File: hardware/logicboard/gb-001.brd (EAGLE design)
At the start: 100 x 75 mm, 2 parts

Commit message: Expanded logicboard.
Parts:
- removed SV1: (no value), con-ml:ML16L
- added SV0: (no value), con-ml:ML34L
- added SV2: (no value), con-ml:ML20L
- added SV3: (no value), con-ml:ML14L
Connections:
- removed net ANLG0R: SV1.3
- removed net ANLG1R: SV1.7
- removed net ANLG2R: SV1.11
- removed net ANLG3R: SV1.15
- removed net DTCT0: SV1.2
- removed net DTCT1: SV1.6
- removed net DTCT2: SV1.10
- removed net DTCT3: SV1.14
- removed net GND: SV1.1, SV1.13, SV1.5, SV1.9
- removed net VCC/2: SV1.12, SV1.16, SV1.4, SV1.8
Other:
- board size 100 x 75 mm -> 100 x 76 mm
- board text added: "Designed for Takachi PF13-3-9"
- board text removed: "Designed for Takachi PF13-4-9"
- board text removed: "GeekPort II"
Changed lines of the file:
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@@
 <setting verticaltext="up"/>
 </settings>
-<grid distance="0.5" unitdist="mm" unit="mm" style="lines" multiple="2" display="yes" altdistance="50" altunitdist="mil" altunit="mil"/>
+<grid distance="1" unitdist="mm" unit="mm" style="lines" multiple="2" display="yes" altdistance="50" altunitdist="mil" altunit="mil"/>
 <layers>
 <layer number="1" name="Top" color="4" fill="1" visible="yes" active="yes"/>
@@
 <layer number="39" name="tKeepout" color="4" fill="11" visible="yes" active="yes"/>
 <layer number="40" name="bKeepout" color="1" fill="11" visible="yes" active="yes"/>
-<layer number="41" name="tRestrict" color="4" fill="10" visible="yes" active="yes"/>
-<layer number="42" name="bRestrict" color="1" fill="10" visible="yes" active="yes"/>
+<layer number="41" name="tRestrict" color="4" fill="10" visible="no" active="yes"/>
+<layer number="42" name="bRestrict" color="1" fill="10" visible="no" active="yes"/>
 <layer number="43" name="vRestrict" color="2" fill="10" visible="yes" active="yes"/>
 <layer number="44" name="Drills" color="7" fill="1" visible="no" active="yes"/>
@@
 <board>
 <plain>
-<wire x1="95" y1="75" x2="5" y2="75" width="0" layer="20"/>
-<wire x1="5" y1="75" x2="4" y2="74" width="0" layer="20" curve="90"/>
-<wire x1="4" y1="74" x2="4" y2="65" width="0" layer="20"/>
+<wire x1="95" y1="75.5" x2="5" y2="75.5" width="0" layer="20"/>
+<wire x1="5" y1="75.5" x2="4" y2="74.5" width="0" layer="20" curve="90"/>
+<wire x1="4" y1="74.5" x2="4" y2="65" width="0" layer="20"/>
 <wire x1="2.5" y1="63.5" x2="1" y2="63.5" width="0" layer="20"/>
 <wire x1="1" y1="63.5" x2="0" y2="62.5" width="0" layer="20" curve="90"/>
@@
 <wire x1="0" y1="12.5" x2="1" y2="11.5" width="0" layer="20" curve="90"/>
 <wire x1="1" y1="11.5" x2="2.5" y2="11.5" width="0" layer="20"/>
-<wire x1="4" y1="10" x2="4" y2="1" width="0" layer="20"/>
-<wire x1="4" y1="1" x2="5" y2="0" width="0" layer="20" curve="90"/>
-<wire x1="5" y1="0" x2="95" y2="0" width="0" layer="20"/>
-<wire x1="95" y1="0" x2="96" y2="1.5" width="0" layer="20" curve="90"/>
-<wire x1="96" y1="1.5" x2="96" y2="10" width="0" layer="20"/>
+<wire x1="4" y1="10" x2="4" y2="0.5" width="0" layer="20"/>
+<wire x1="4" y1="0.5" x2="5" y2="-0.5" width="0" layer="20" curve="90"/>
+<wire x1="5" y1="-0.5" x2="95" y2="-0.5" width="0" layer="20"/>
+<wire x1="95" y1="-0.5" x2="96" y2="0.5" width="0" layer="20" curve="90"/>
+<wire x1="96" y1="0.5" x2="96" y2="10" width="0" layer="20"/>
 <wire x1="97.5" y1="11.5" x2="99" y2="11.5" width="0" layer="20"/>
 <wire x1="99" y1="11.5" x2="100" y2="12.5" width="0" layer="20" curve="90"/>
@@
 <wire x1="100" y1="62.5" x2="99" y2="63.5" width="0" layer="20" curve="90"/>
 <wire x1="99" y1="63.5" x2="97.5" y2="63.5" width="0" layer="20"/>
-<wire x1="96" y1="65" x2="96" y2="74" width="0" layer="20"/>
-<wire x1="96" y1="74" x2="95" y2="75" width="0" layer="20" curve="90"/>
+<wire x1="96" y1="65" x2="96" y2="74.5" width="0" layer="20"/>
+<wire x1="96" y1="74.5" x2="95" y2="75.5" width="0" layer="20" curve="90"/>
 <hole x="93.5" y="61" drill="2.5"/>
 <circle x="6.5" y="14" radius="2" width="0.2" layer="42"/>
@@
 <text x="4.5" y="6" size="1" layer="25" align="center-left">Designed for
 Takachi
-PF13-4-9</text>
-<text x="90" y="70.5" size="1" layer="25" rot="R90" align="center">GeekPort II</text>
-<hole x="87.5" y="70.5" drill="2.7"/>
-<hole x="62.5" y="70.5" drill="2.7"/>
-<circle x="87.5" y="70.5" radius="2" width="0.2" layer="41"/>
-<circle x="62.5" y="70.5" radius="2" width="0.2" layer="41"/>
-<circle x="87.5" y="70.5" radius="2" width="0.2" layer="42"/>
-<circle x="62.5" y="70.5" radius="2" width="0.2" layer="42"/>
+PF13-3-9</text>
 <text x="93.5" y="11.5" size="1" layer="25" align="center">4-M2.3</text>
 </plain>
@@
 <elements>
 <element name="U$1" library="pineapple" package="PINEAPPLE450_SILK" value="PINEAPPLE450_SILK" x="8.5" y="34" smashed="yes"/>
-<element name="SV1" library="con-ml" library_urn="urn:adsk.eagle:library:164" package="ML16L" package3d_urn="urn:adsk.eagle:package:8682/1" value="" x="75" y="64" smashed="yes">
-<attribute name="MF" value="" x="75" y="64" size="1.778" layer="27" display="off"/>
-<attribute name="MPN" value="" x="75" y="64" size="1.778" layer="27" display="off"/>
-<attribute name="NAME" x="87.5" y="64" size="1" layer="25" ratio="10" align="center"/>
-<attribute name="OC_FARNELL" value="unknown" x="75" y="64" size="1.778" layer="27" display="off"/>
-<attribute name="OC_NEWARK" value="unknown" x="75" y="64" size="1.778" layer="27" display="off"/>
-<attribute name="POPULARITY" value="0" x="75" y="64" size="1.778" layer="27" display="off"/>
-<attribute name="VALUE" x="74.9746" y="75.43" size="1.778" layer="27" ratio="10"/>
+<element name="SV0" library="con-ml" library_urn="urn:adsk.eagle:library:164" package="ML34L" package3d_urn="urn:adsk.eagle:package:8689/1" value="" x="50" y="11" smashed="yes" rot="R180">
+<attribute name="MF" value="" x="50" y="11" size="1.778" layer="27" rot="R180" display="off"/>
+<attribute name="MPN" value="" x="50" y="11" size="1.778" layer="27" rot="R180" display="off"/>
+<attribute name="NAME" x="75.4254" y="-0.43" size="1.778" layer="25" ratio="10" rot="R180"/>
+<attribute name="OC_FARNELL" value="unknown" x="50" y="11" size="1.778" layer="27" rot="R180" display="off"/>
+<attribute name="OC_NEWARK" value="unknown" x="50" y="11" size="1.778" layer="27" rot="R180" display="off"/>
+<attribute name="POPULARITY" value="0" x="50" y="11" size="1.778" layer="27" rot="R180" display="off"/>
+<attribute name="VALUE" x="60.1854" y="-0.43" size="1.778" layer="27" ratio="10" rot="R180"/>
+</element>
+<element name="SV2" library="con-ml" library_urn="urn:adsk.eagle:library:164" package="ML20L" package3d_urn="urn:adsk.eagle:package:8685/1" value="" x="29" y="64" smashed="yes">
+<attribute name="MF" value="" x="29" y="64" size="1.778" layer="27" display="off"/>
+<attribute name="MPN" value="" x="29" y="64" size="1.778" layer="27" display="off"/>
+<attribute name="NAME" x="12.4646" y="75.43" size="1.778" layer="25" ratio="10"/>
+<attribute name="OC_FARNELL" value="unknown" x="29" y="64" size="1.778" layer="27" display="off"/>
+<attribute name="OC_NEWARK" value="unknown" x="29" y="64" size="1.778" layer="27" display="off"/>
+<attribute name="POPULARITY" value="0" x="29" y="64" size="1.778" layer="27" display="off"/>
+<attribute name="VALUE" x="23.8946" y="75.43" size="1.778" layer="27" ratio="10"/>
+</element>
+<element name="SV3" library="con-ml" library_urn="urn:adsk.eagle:library:164" package="ML14L" package3d_urn="urn:adsk.eagle:package:8677/1" value="" x="76" y="64" smashed="yes">
+<attribute name="MF" value="" x="76" y="64" size="1.778" layer="27" display="off"/>
+<attribute name="MPN" value="" x="76" y="64" size="1.778" layer="27" display="off"/>
+<attribute name="NAME" x="63.2746" y="75.43" size="1.778" layer="25" ratio="10"/>
+<attribute name="OC_FARNELL" value="unknown" x="76" y="64" size="1.778" layer="27" display="off"/>
+<attribute name="OC_NEWARK" value="unknown" x="76" y="64" size="1.778" layer="27" display="off"/>
+<attribute name="POPULARITY" value="0" x="76" y="64" size="1.778" layer="27" display="off"/>
+<attribute name="VALUE" x="75.9746" y="75.43" size="1.778" layer="27" ratio="10"/>
 </element>
 </elements>
 <signals>
-<signal name="GND" class="1">
-<contactref element="SV1" pad="1"/>
-<contactref element="SV1" pad="5"/>
-<contactref element="SV1" pad="9"/>
-<contactref element="SV1" pad="13"/>
-<wire x1="76.27" y1="62.73" x2="81.35" y2="62.73" width="0" layer="19" extent="1-1"/>
-<wire x1="71.19" y1="62.73" x2="76.27" y2="62.73" width="0" layer="19" extent="1-1"/>
-<wire x1="66.11" y1="62.73" x2="71.19" y2="62.73" width="0" layer="19" extent="1-1"/>
-</signal>
-<signal name="DTCT0">
-<contactref element="SV1" pad="2"/>
-</signal>
-<signal name="DTCT1">
-<contactref element="SV1" pad="6"/>
-</signal>
-<signal name="DTCT2">
-<contactref element="SV1" pad="10"/>
-</signal>
-<signal name="DTCT3">
-<contactref element="SV1" pad="14"/>
-</signal>
-<signal name="VCC/2" class="4">
-<contactref element="SV1" pad="4"/>
-<contactref element="SV1" pad="8"/>
-<contactref element="SV1" pad="12"/>
-<contactref element="SV1" pad="16"/>
-<wire x1="78.81" y1="65.27" x2="83.89" y2="65.27" width="0" layer="19" extent="1-1"/>
-<wire x1="73.73" y1="65.27" x2="78.81" y2="65.27" width="0" layer="19" extent="1-1"/>
-<wire x1="68.65" y1="65.27" x2="73.73" y2="65.27" width="0" layer="19" extent="1-1"/>
-</signal>
-<signal name="ANLG0R" class="3">
-<contactref element="SV1" pad="3"/>
-</signal>
-<signal name="ANLG1R" class="3">
-<contactref element="SV1" pad="7"/>
-</signal>
-<signal name="ANLG2R" class="3">
-<contactref element="SV1" pad="11"/>
-</signal>
-<signal name="ANLG3R" class="3">
-<contactref element="SV1" pad="15"/>
-</signal>
 </signals>
 <mfgpreviewcolors>

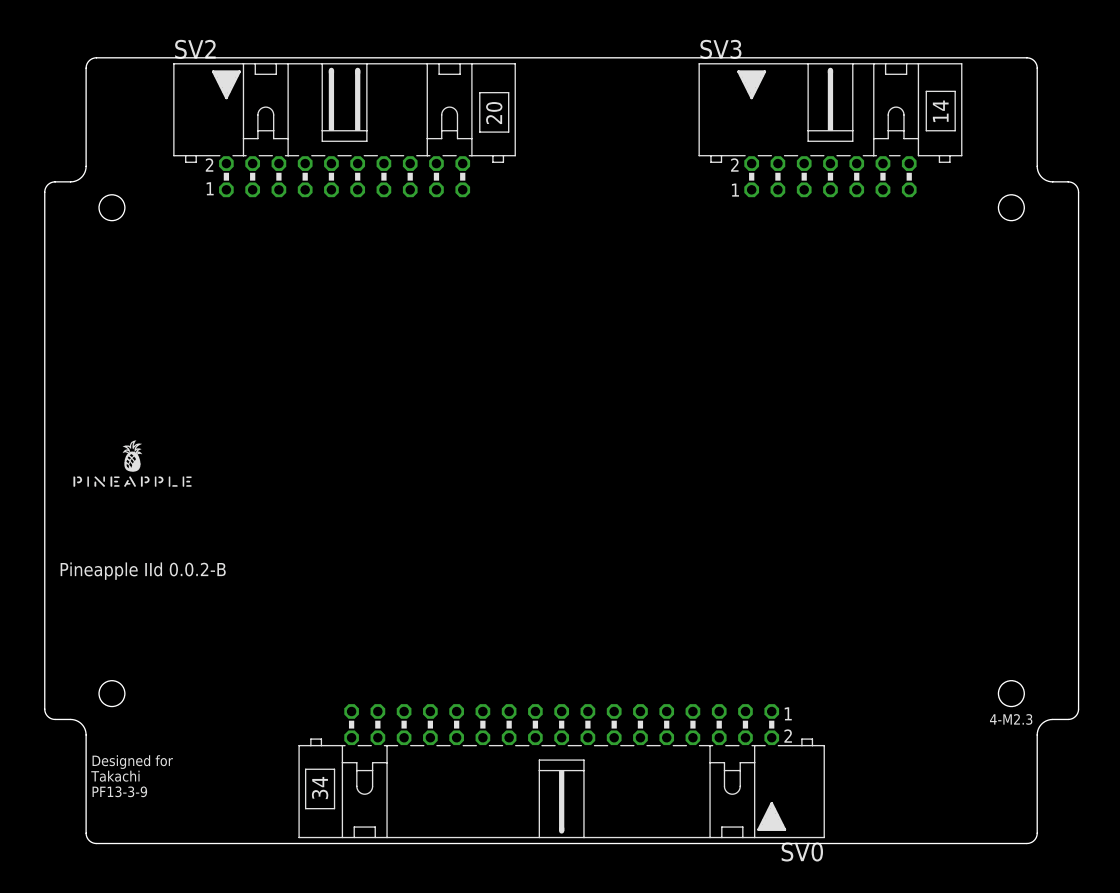
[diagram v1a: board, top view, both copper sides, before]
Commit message: Re-centered logicboard.
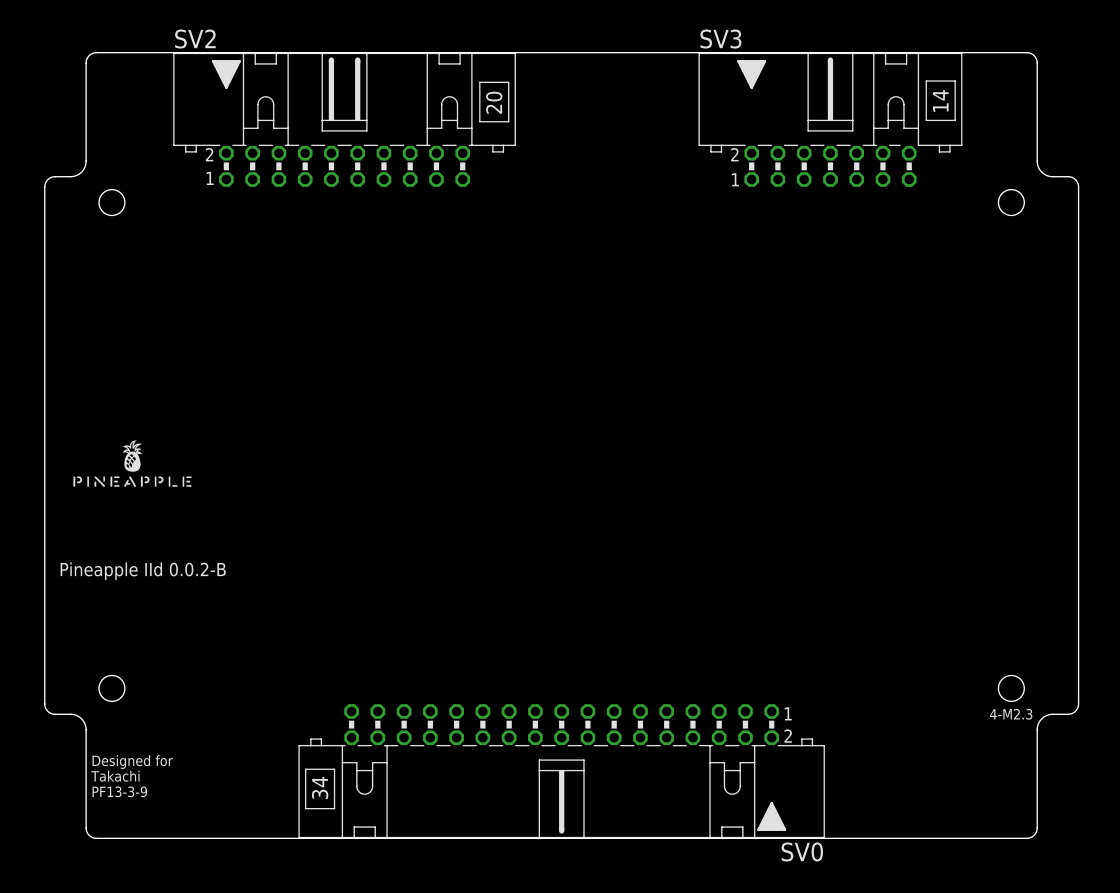
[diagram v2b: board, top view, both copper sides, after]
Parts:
- moved SV2 1.00 mm to (29.0, 65.0)
- moved SV3 1.00 mm to (76.0, 65.0)
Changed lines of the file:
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@@
 <layer number="39" name="tKeepout" color="4" fill="11" visible="yes" active="yes"/>
 <layer number="40" name="bKeepout" color="1" fill="11" visible="yes" active="yes"/>
-<layer number="41" name="tRestrict" color="4" fill="10" visible="no" active="yes"/>
-<layer number="42" name="bRestrict" color="1" fill="10" visible="no" active="yes"/>
+<layer number="41" name="tRestrict" color="4" fill="10" visible="yes" active="yes"/>
+<layer number="42" name="bRestrict" color="1" fill="10" visible="yes" active="yes"/>
 <layer number="43" name="vRestrict" color="2" fill="10" visible="yes" active="yes"/>
 <layer number="44" name="Drills" color="7" fill="1" visible="no" active="yes"/>
@@
 <board>
 <plain>
-<wire x1="95" y1="75.5" x2="5" y2="75.5" width="0" layer="20"/>
-<wire x1="5" y1="75.5" x2="4" y2="74.5" width="0" layer="20" curve="90"/>
-<wire x1="4" y1="74.5" x2="4" y2="65" width="0" layer="20"/>
-<wire x1="2.5" y1="63.5" x2="1" y2="63.5" width="0" layer="20"/>
-<wire x1="1" y1="63.5" x2="0" y2="62.5" width="0" layer="20" curve="90"/>
-<wire x1="0" y1="62.5" x2="0" y2="12.5" width="0" layer="20"/>
-<wire x1="0" y1="12.5" x2="1" y2="11.5" width="0" layer="20" curve="90"/>
-<wire x1="1" y1="11.5" x2="2.5" y2="11.5" width="0" layer="20"/>
-<wire x1="4" y1="10" x2="4" y2="0.5" width="0" layer="20"/>
-<wire x1="4" y1="0.5" x2="5" y2="-0.5" width="0" layer="20" curve="90"/>
-<wire x1="5" y1="-0.5" x2="95" y2="-0.5" width="0" layer="20"/>
-<wire x1="95" y1="-0.5" x2="96" y2="0.5" width="0" layer="20" curve="90"/>
-<wire x1="96" y1="0.5" x2="96" y2="10" width="0" layer="20"/>
-<wire x1="97.5" y1="11.5" x2="99" y2="11.5" width="0" layer="20"/>
-<wire x1="99" y1="11.5" x2="100" y2="12.5" width="0" layer="20" curve="90"/>
-<wire x1="100" y1="12.5" x2="100" y2="62.5" width="0" layer="20"/>
-<wire x1="100" y1="62.5" x2="99" y2="63.5" width="0" layer="20" curve="90"/>
-<wire x1="99" y1="63.5" x2="97.5" y2="63.5" width="0" layer="20"/>
-<wire x1="96" y1="65" x2="96" y2="74.5" width="0" layer="20"/>
-<wire x1="96" y1="74.5" x2="95" y2="75.5" width="0" layer="20" curve="90"/>
-<hole x="93.5" y="61" drill="2.5"/>
-<circle x="6.5" y="14" radius="2" width="0.2" layer="42"/>
-<circle x="93.5" y="14" radius="2" width="0.2" layer="42"/>
-<circle x="93.5" y="61" radius="2" width="0.2" layer="42"/>
-<circle x="6.5" y="61" radius="2" width="0.2" layer="42"/>
-<circle x="6.5" y="61" radius="2" width="0.2" layer="41"/>
-<circle x="93.5" y="61" radius="2" width="0.2" layer="41"/>
-<circle x="6.5" y="14" radius="2" width="0.2" layer="41"/>
-<circle x="93.5" y="14" radius="2" width="0.2" layer="41"/>
+<wire x1="95" y1="76" x2="5" y2="76" width="0" layer="20"/>
+<wire x1="5" y1="76" x2="4" y2="75" width="0" layer="20" curve="90"/>
+<wire x1="4" y1="75" x2="4" y2="65.5" width="0" layer="20"/>
+<wire x1="2.5" y1="64" x2="1" y2="64" width="0" layer="20"/>
+<wire x1="1" y1="64" x2="0" y2="63" width="0" layer="20" curve="90"/>
+<wire x1="0" y1="63" x2="0" y2="13" width="0" layer="20"/>
+<wire x1="0" y1="13" x2="1" y2="12" width="0" layer="20" curve="90"/>
+<wire x1="1" y1="12" x2="2.5" y2="12" width="0" layer="20"/>
+<wire x1="4" y1="10.5" x2="4" y2="1" width="0" layer="20"/>
+<wire x1="4" y1="1" x2="5" y2="0" width="0" layer="20" curve="90"/>
+<wire x1="5" y1="0" x2="95" y2="0" width="0" layer="20"/>
+<wire x1="95" y1="0" x2="96" y2="1" width="0" layer="20" curve="90"/>
+<wire x1="96" y1="1" x2="96" y2="10.5" width="0" layer="20"/>
+<wire x1="97.5" y1="12" x2="99" y2="12" width="0" layer="20"/>
+<wire x1="99" y1="12" x2="100" y2="13" width="0" layer="20" curve="90"/>
+<wire x1="100" y1="13" x2="100" y2="63" width="0" layer="20"/>
+<wire x1="100" y1="63" x2="99" y2="64" width="0" layer="20" curve="90"/>
+<wire x1="99" y1="64" x2="97.5" y2="64" width="0" layer="20"/>
+<wire x1="96" y1="65.5" x2="96" y2="75" width="0" layer="20"/>
+<wire x1="96" y1="75" x2="95" y2="76" width="0" layer="20" curve="90"/>
+<hole x="93.5" y="61.5" drill="2.5"/>
+<circle x="6.5" y="14.5" radius="2" width="0.2" layer="42"/>
+<circle x="93.5" y="14.5" radius="2" width="0.2" layer="42"/>
+<circle x="93.5" y="61.5" radius="2" width="0.2" layer="42"/>
+<circle x="6.5" y="61.5" radius="2" width="0.2" layer="42"/>
+<circle x="6.5" y="61.5" radius="2" width="0.2" layer="41"/>
+<circle x="93.5" y="61.5" radius="2" width="0.2" layer="41"/>
+<circle x="6.5" y="14.5" radius="2" width="0.2" layer="41"/>
+<circle x="93.5" y="14.5" radius="2" width="0.2" layer="41"/>
 <text x="9.5" y="26" size="1.27" layer="25" align="center">Pineapple IId 0.0.2-B</text>
-<wire x1="96" y1="65" x2="97.5" y2="63.5" width="0" layer="20" curve="90"/>
-<wire x1="4" y1="65" x2="2.5" y2="63.5" width="0" layer="20" curve="-90"/>
-<wire x1="96" y1="10" x2="97.5" y2="11.5" width="0" layer="20" curve="-90"/>
-<wire x1="2.5" y1="11.5" x2="4" y2="10" width="0" layer="20" curve="-90"/>
-<hole x="6.5" y="61" drill="2.5"/>
-<hole x="6.5" y="14" drill="2.5"/>
-<hole x="93.5" y="14" drill="2.5"/>
+<wire x1="96" y1="65.5" x2="97.5" y2="64" width="0" layer="20" curve="90"/>
+<wire x1="4" y1="65.5" x2="2.5" y2="64" width="0" layer="20" curve="-90"/>
+<wire x1="96" y1="10.5" x2="97.5" y2="12" width="0" layer="20" curve="-90"/>
+<wire x1="2.5" y1="12" x2="4" y2="10.5" width="0" layer="20" curve="-90"/>
+<hole x="6.5" y="61.5" drill="2.5"/>
+<hole x="6.5" y="14.5" drill="2.5"/>
+<hole x="93.5" y="14.5" drill="2.5"/>
 <rectangle x1="4" y1="74" x2="96" y2="75" layer="41"/>
 <rectangle x1="99" y1="11.5" x2="100" y2="63.5" layer="41"/>
@@
 Takachi
 PF13-3-9</text>
-<text x="93.5" y="11.5" size="1" layer="25" align="center">4-M2.3</text>
+<text x="93.5" y="12" size="1" layer="25" align="center">4-M2.3</text>
 </plain>
 <attributes>
@@
 <attribute name="VALUE" x="60.1854" y="-0.43" size="1.778" layer="27" ratio="10" rot="R180"/>
 </element>
-<element name="SV2" library="con-ml" library_urn="urn:adsk.eagle:library:164" package="ML20L" package3d_urn="urn:adsk.eagle:package:8685/1" value="" x="29" y="64" smashed="yes">
-<attribute name="MF" value="" x="29" y="64" size="1.778" layer="27" display="off"/>
-<attribute name="MPN" value="" x="29" y="64" size="1.778" layer="27" display="off"/>
-<attribute name="NAME" x="12.4646" y="75.43" size="1.778" layer="25" ratio="10"/>
-<attribute name="OC_FARNELL" value="unknown" x="29" y="64" size="1.778" layer="27" display="off"/>
-<attribute name="OC_NEWARK" value="unknown" x="29" y="64" size="1.778" layer="27" display="off"/>
-<attribute name="POPULARITY" value="0" x="29" y="64" size="1.778" layer="27" display="off"/>
-<attribute name="VALUE" x="23.8946" y="75.43" size="1.778" layer="27" ratio="10"/>
+<element name="SV2" library="con-ml" library_urn="urn:adsk.eagle:library:164" package="ML20L" package3d_urn="urn:adsk.eagle:package:8685/1" value="" x="29" y="65" smashed="yes">
+<attribute name="MF" value="" x="29" y="65" size="1.778" layer="27" display="off"/>
+<attribute name="MPN" value="" x="29" y="65" size="1.778" layer="27" display="off"/>
+<attribute name="NAME" x="12.4646" y="76.43" size="1.778" layer="25" ratio="10"/>
+<attribute name="OC_FARNELL" value="unknown" x="29" y="65" size="1.778" layer="27" display="off"/>
+<attribute name="OC_NEWARK" value="unknown" x="29" y="65" size="1.778" layer="27" display="off"/>
+<attribute name="POPULARITY" value="0" x="29" y="65" size="1.778" layer="27" display="off"/>
+<attribute name="VALUE" x="23.8946" y="76.43" size="1.778" layer="27" ratio="10"/>
 </element>
-<element name="SV3" library="con-ml" library_urn="urn:adsk.eagle:library:164" package="ML14L" package3d_urn="urn:adsk.eagle:package:8677/1" value="" x="76" y="64" smashed="yes">
-<attribute name="MF" value="" x="76" y="64" size="1.778" layer="27" display="off"/>
-<attribute name="MPN" value="" x="76" y="64" size="1.778" layer="27" display="off"/>
-<attribute name="NAME" x="63.2746" y="75.43" size="1.778" layer="25" ratio="10"/>
-<attribute name="OC_FARNELL" value="unknown" x="76" y="64" size="1.778" layer="27" display="off"/>
-<attribute name="OC_NEWARK" value="unknown" x="76" y="64" size="1.778" layer="27" display="off"/>
-<attribute name="POPULARITY" value="0" x="76" y="64" size="1.778" layer="27" display="off"/>
-<attribute name="VALUE" x="75.9746" y="75.43" size="1.778" layer="27" ratio="10"/>
+<element name="SV3" library="con-ml" library_urn="urn:adsk.eagle:library:164" package="ML14L" package3d_urn="urn:adsk.eagle:package:8677/1" value="" x="76" y="65" smashed="yes">
+<attribute name="MF" value="" x="76" y="65" size="1.778" layer="27" display="off"/>
+<attribute name="MPN" value="" x="76" y="65" size="1.778" layer="27" display="off"/>
+<attribute name="NAME" x="63.2746" y="76.43" size="1.778" layer="25" ratio="10"/>
+<attribute name="OC_FARNELL" value="unknown" x="76" y="65" size="1.778" layer="27" display="off"/>
+<attribute name="OC_NEWARK" value="unknown" x="76" y="65" size="1.778" layer="27" display="off"/>
+<attribute name="POPULARITY" value="0" x="76" y="65" size="1.778" layer="27" display="off"/>
+<attribute name="VALUE" x="75.9746" y="76.43" size="1.778" layer="27" ratio="10"/>
 </element>
 </elements>
